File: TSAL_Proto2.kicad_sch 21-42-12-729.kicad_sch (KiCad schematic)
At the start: 29 parts, among them J1 043045-0412, Q1 DMP2035U-7, Q3 UJ3N065080K3S, Q4 DMN2056U, Q5 AO3400A, U1 H11L1M, U2 NE555D

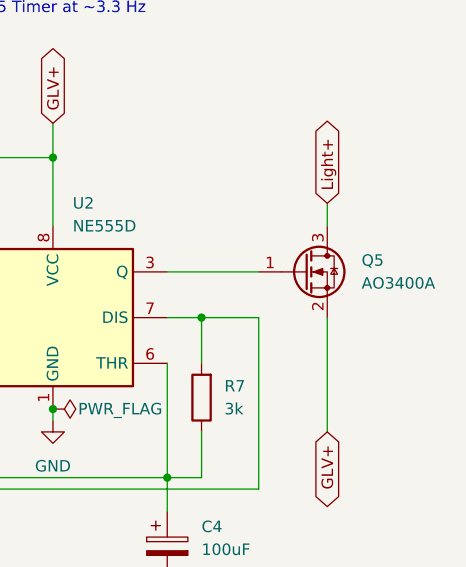
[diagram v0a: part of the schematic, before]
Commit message: added working 555 sim
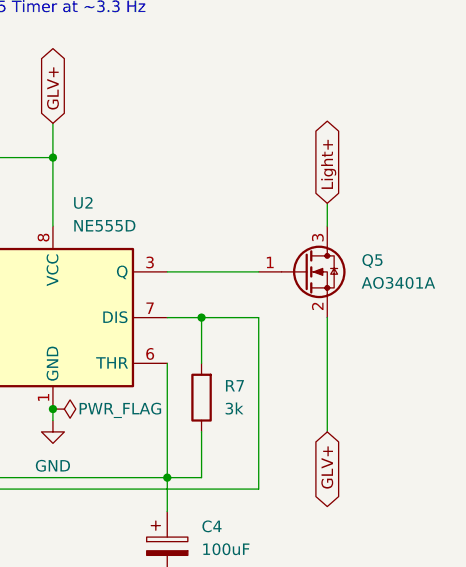
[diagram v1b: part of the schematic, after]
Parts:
- Q5: value AO3400A -> AO3401A
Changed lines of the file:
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@@
 			)
 		)
-		(property "Value" "AO3400A"
+		(property "Value" "AO3401A"
 			(at 187.96 55.8799 0)
 			(effects
